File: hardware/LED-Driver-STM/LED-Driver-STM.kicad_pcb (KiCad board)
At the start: 2 copper layers, 64.8 x 64.8 mm, 103 parts, among them J1 I2C4, J2 IO5, J3 PWR, J4 PROG5, J5 ADC2, J6 INT2, J7 INT2, J8 ADC3, Q1 2N7002, Q10 2N7002, Q11 2N7002, Q12 2N7002, Q13 2N7002, Q14 2N7002, Q15 2N7002, Q16 2N7002, Q17 2N7002, Q18 2N7002, Q19 2N7002, Q2 2N7002, Q20 2N7002, Q3 2N7002, Q4 2N7002, Q5 2N7002, Q6 2N7002, Q7 2N7002, Q8 2N7002, Q9 2N7002, SW1 SPT, SW2 SPT, SW3 SPT, U1 STM32F030C8Tx, U2 AMS1117-3.3, U3 L3GD20, U4 LIS3DH, Y1 16MHz

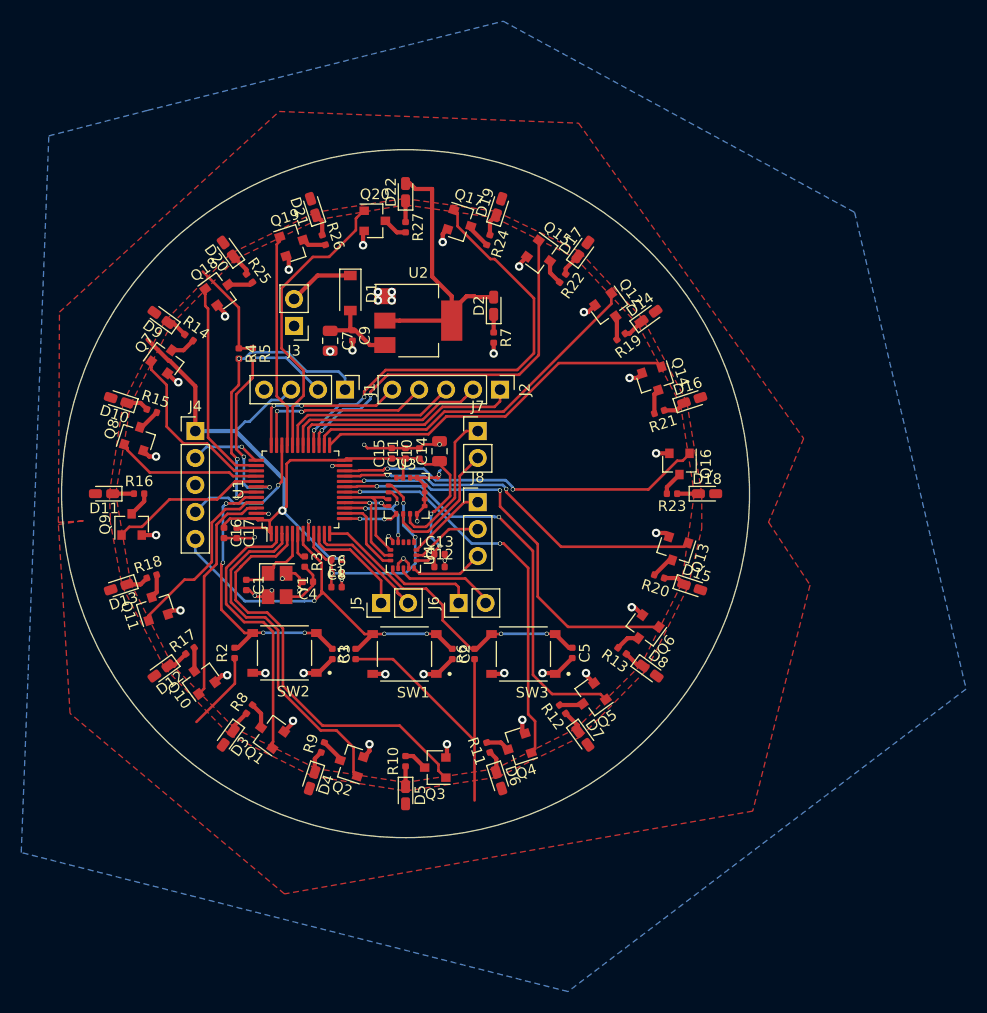
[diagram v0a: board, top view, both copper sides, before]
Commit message: Latest board layout
This is the board that was purchased
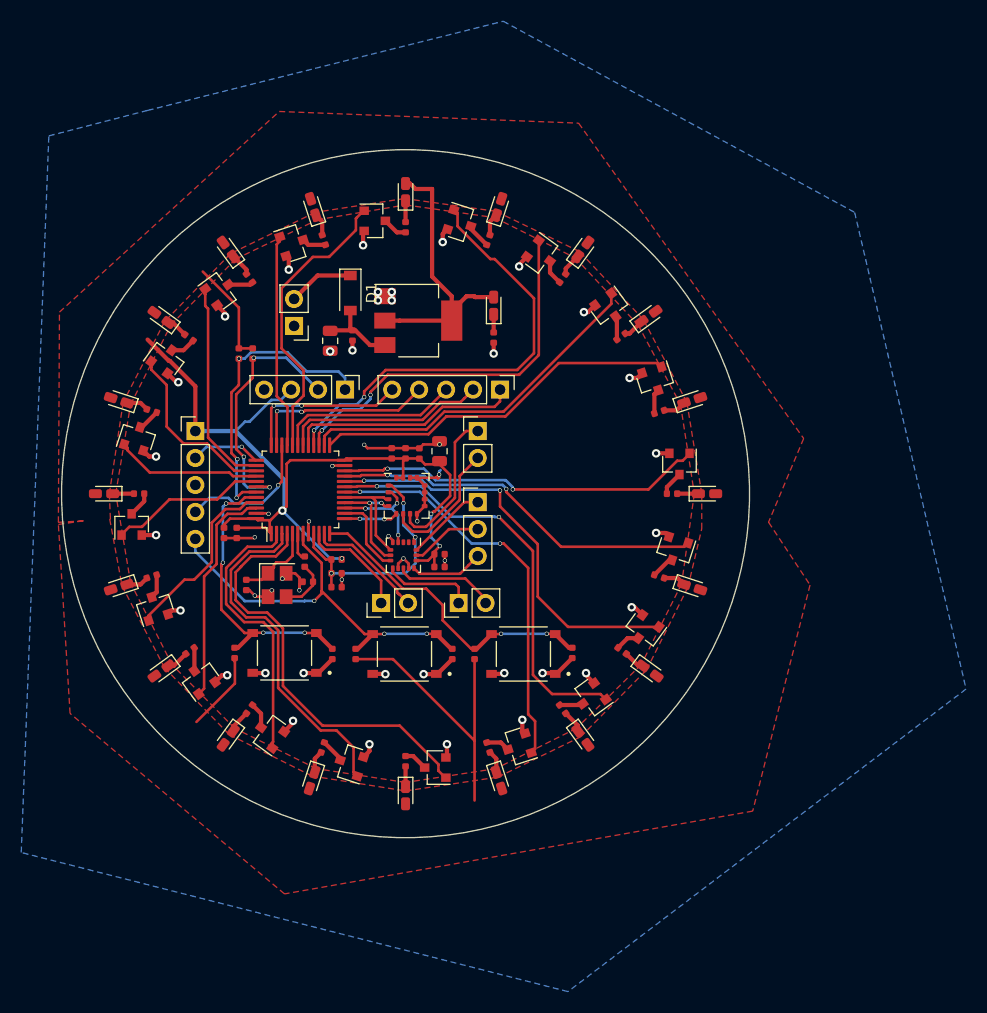
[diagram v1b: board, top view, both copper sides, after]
